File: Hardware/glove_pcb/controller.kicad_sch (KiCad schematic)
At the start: 17 parts, among them J10 ICSP, J11 IMU, J12 IMU, J9 Debug Serial, U10 MCP3008, U11 MCP3008, U8 MCP3008, U9 ATmega328PB-A

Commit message: Made most of changes from meeting
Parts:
- added C44: 0.1uF, Capacitor_SMD:C_0603_1608Metric_Pad1.08x0.95mm_HandSolder, symbol Device:C
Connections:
- net VCC_UC renamed +5V

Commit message: Finish changes according to feedback
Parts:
- removed C32: 0.1uF, Capacitor_SMD:C_0603_1608Metric_Pad1.08x0.95mm_HandSolder, symbol Device:C
- removed C33: 10uF, Capacitor_SMD:C_1206_3216Metric_Pad1.33x1.80mm_HandSolder, symbol Device:C
- added C30, C35, C36, C37, C38, C39, C40, C41, C42, C45, C46, C49, C50, C51: 0.1uF, symbol Device:C_Small
- added C43: 0.1uF, Capacitor_SMD:C_0603_1608Metric_Pad1.08x0.95mm_HandSolder, symbol Device:C
- added SW2: SW_Push, symbol Switch:SW_Push
- C44: value 0.1uF -> 10uF; footprint Capacitor_SMD:C_0603_1608Metric_Pad1.08x0.95mm_HandSolder -> Capacitor_SMD:C_1206_3216Metric_Pad1.33x1.80mm_HandSolder
- renumbered C30 to C31, C31 to C32, C28 to C33, C29 to C34, C34 to C47, C35 to C48, R34 to R30
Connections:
- net +5V: now also C44.1, C43.1
- net GND: now also C44.2, U10.7 (CH6), U10.8 (CH7), C30.1, C35.1, C36.1, C37.1, C38.1, C39.1, C40.1, C41.1, C42.1, C43.2, C45.1, C46.1, C49.1, C50.1, C51.1, SW2.2
- net POT_INDEX_1: now also C36.2
- net POT_INDEX_2: now also C37.2
- net POT_INDEX_3: now also C38.2
- net POT_MIDDLE_1: now also C39.2
- net POT_MIDDLE_2: now also C40.2
- net POT_MIDDLE_3: now also C41.2
- net POT_PINKY_1: now also C49.2
- net POT_PINKY_2: now also C50.2
- net POT_PINKY_3: now also C51.2
- net POT_RING_1: now also C42.2
- net POT_RING_2: now also C45.2
- net POT_RING_3: now also C46.2
- net POT_THUMB_1: now also C30.2
- net POT_THUMB_2: now also C35.2
- net UC_MOTOR_PMODE: no longer names the net of U9.11 (PD7)
- net UC_MOTOR_PMODE: now also SW2.1
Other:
- note added: "Emergency Stop"
- moved on the sheet: C33, C34, C47, C48, J11, J12, U11, U8

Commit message: Finish schematic updates
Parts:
- removed J10: ICSP, Connector_PinSocket_2.54mm:PinSocket_2x03_P2.54mm_Vertical, symbol Connector_Generic:Conn_02x03_Top_Bottom
- added J10: AVR-ISP-6, symbol Connector:AVR-ISP-6
- renumbered U8 to U12, U9 to U13, U10 to U14, U11 to U15
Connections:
- net +5V: now also J10.2 (VCC)
- net GND: now also J10.6 (GND)
- net MISO: now also J10.1 (MISO)
- net MOSI: now also J10.4 (MOSI)
- net RST: now also J10.5 (~{RST})
- net SCK: now also J10.3 (SCK)

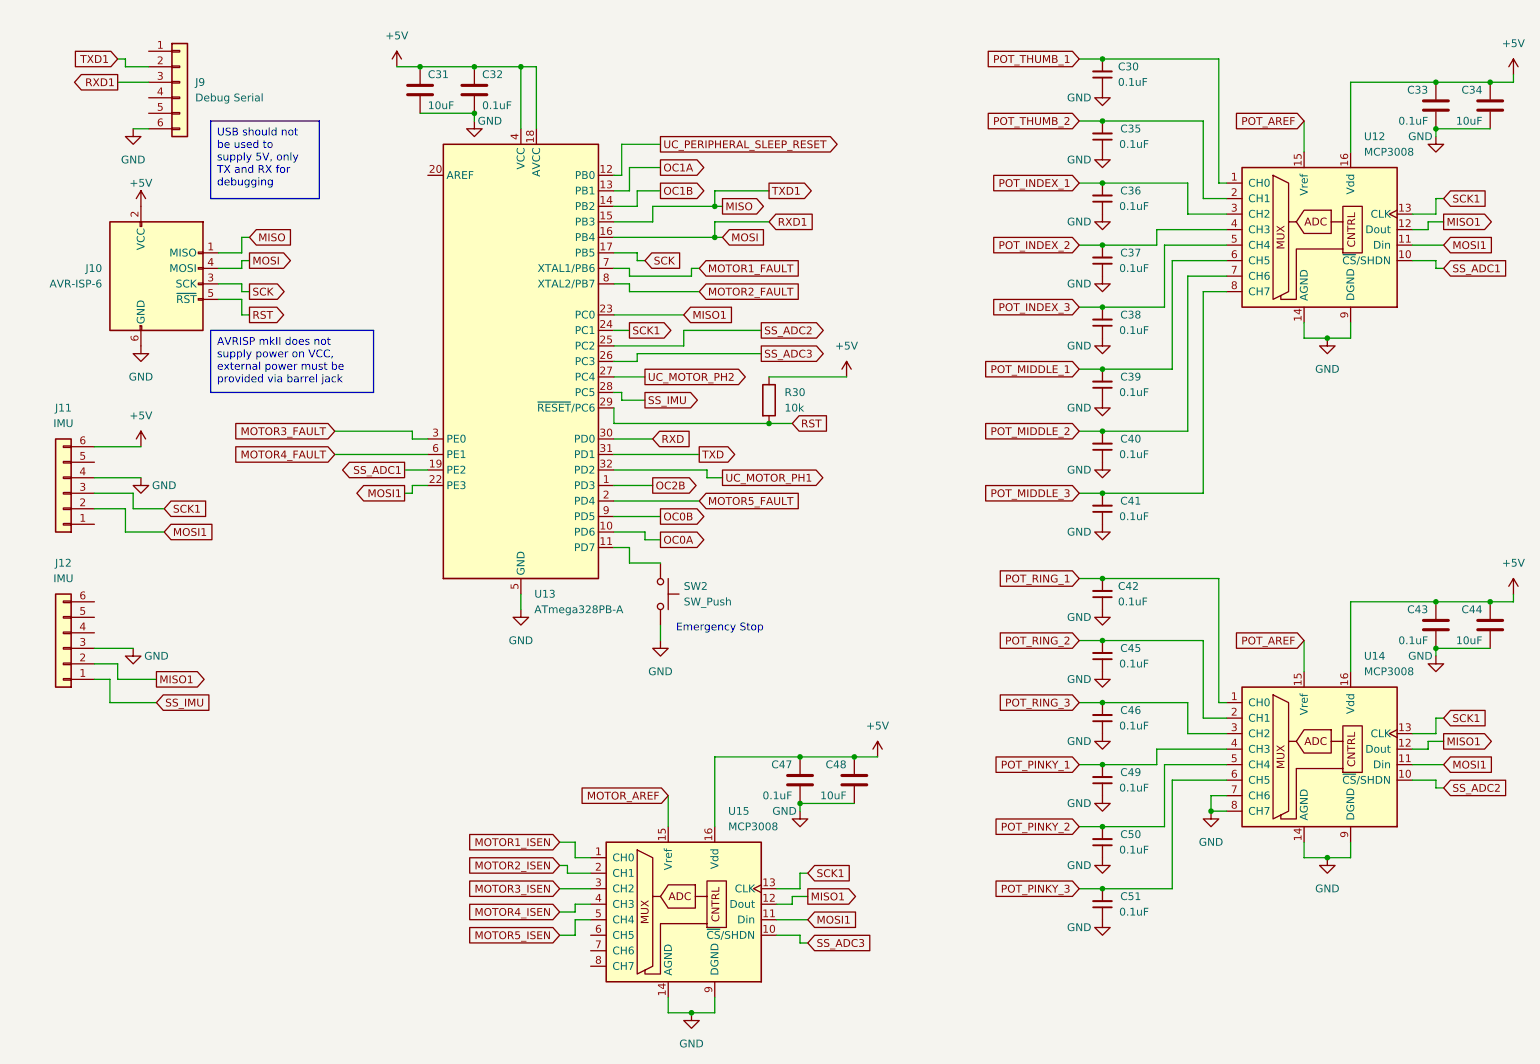
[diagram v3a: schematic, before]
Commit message: More updates to the schematic based on Dmitry's feedback
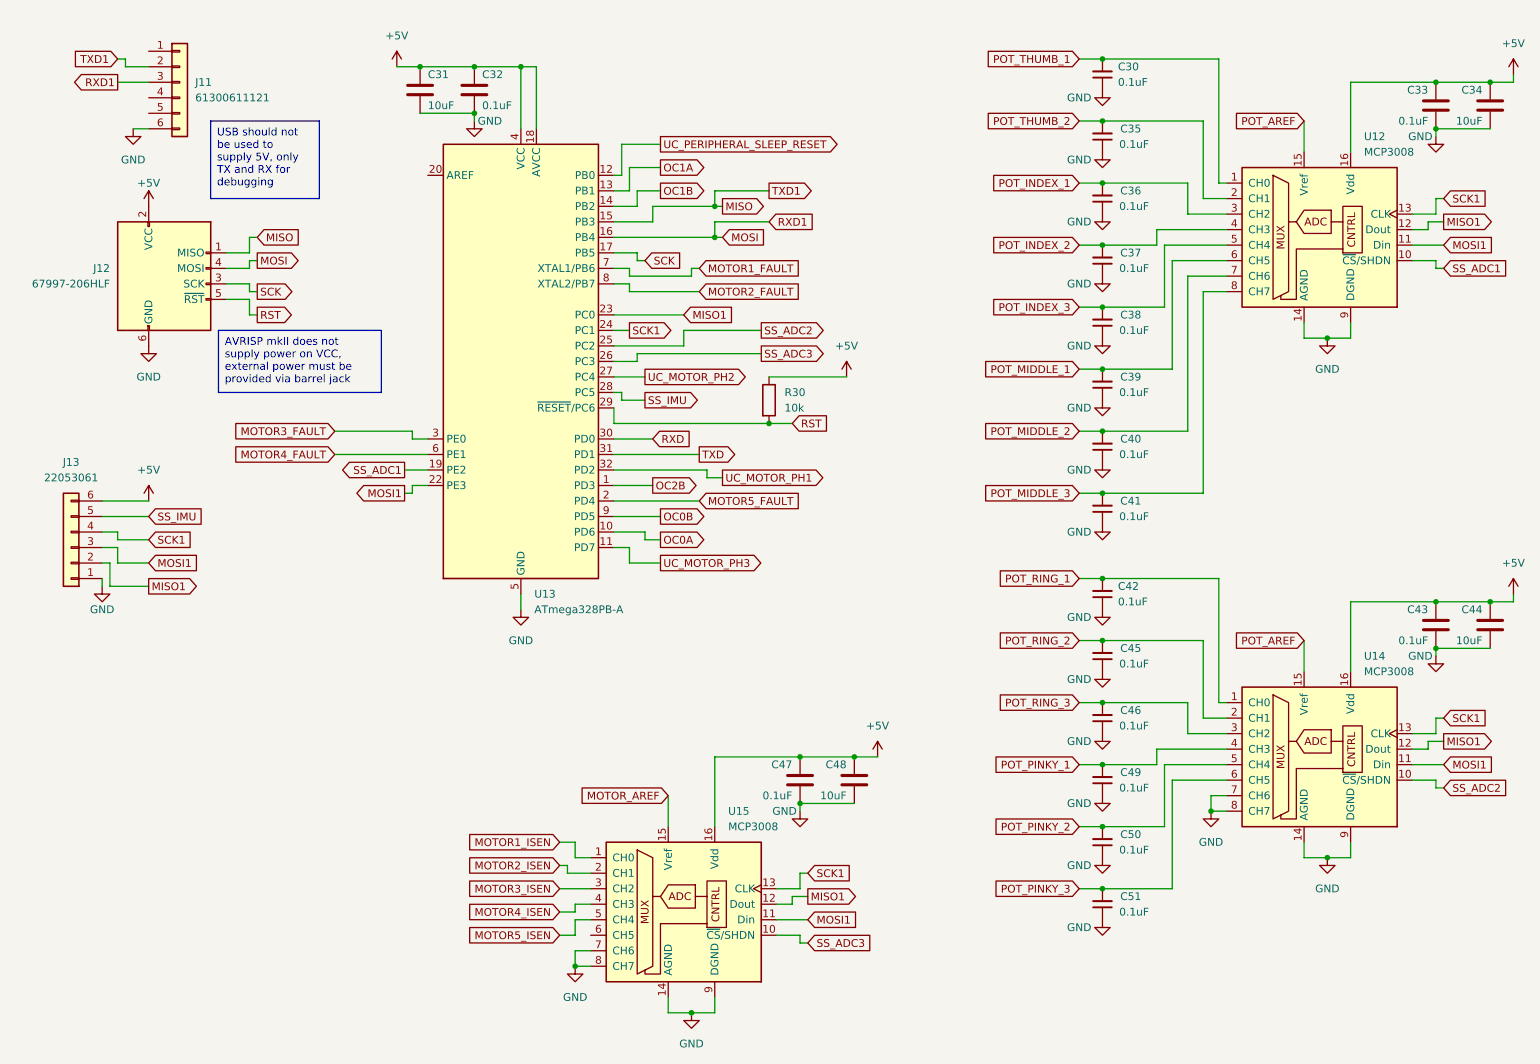
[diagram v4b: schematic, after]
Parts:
- removed J12: IMU, Connector_PinSocket_2.54mm:PinSocket_1x06_P2.54mm_Vertical, symbol Connector_Generic:Conn_01x06
- removed SW2: SW_Push, symbol Switch:SW_Push
- J11: renamed from J9; value Debug Serial -> 61300611121
- J12: renamed from J10; value AVR-ISP-6 -> 67997-206HLF
- J13: renamed from J11; value IMU -> 22053061
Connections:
- net GND: now also J13.1 (Pin_1), U15.7 (CH6), U15.8 (CH7); no longer J13.4 (Pin_4)
- net MISO1: now also J13.2 (Pin_2)
- net MOSI1: now also J13.3 (Pin_3); no longer J13.2 (Pin_2)
- net SCK1: now also J13.4 (Pin_4); no longer J13.3 (Pin_3)
- net SS_IMU: now also J13.5 (Pin_5)
- net UC_MOTOR_PH3: now reaches U13.11 (PD7)
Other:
- note removed: "Emergency Stop"
- moved on the sheet: J12, J13

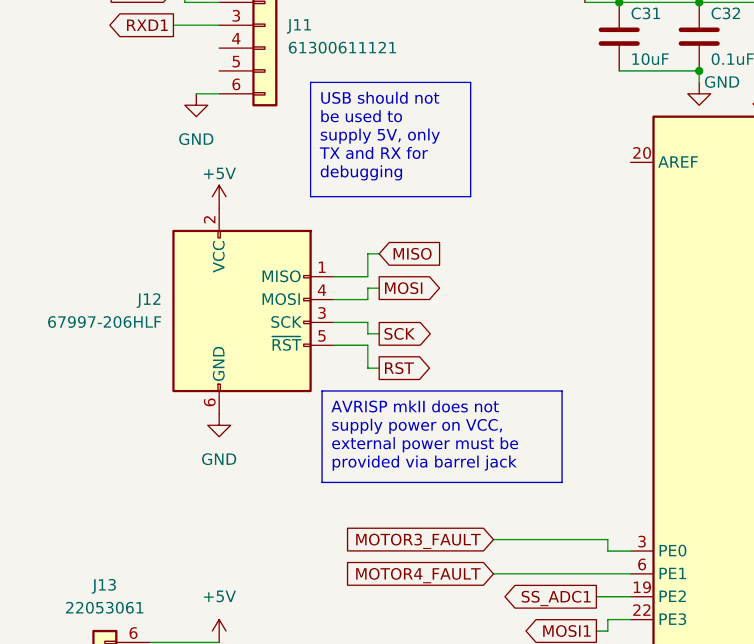
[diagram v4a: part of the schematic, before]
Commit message: Change isp pin symbol
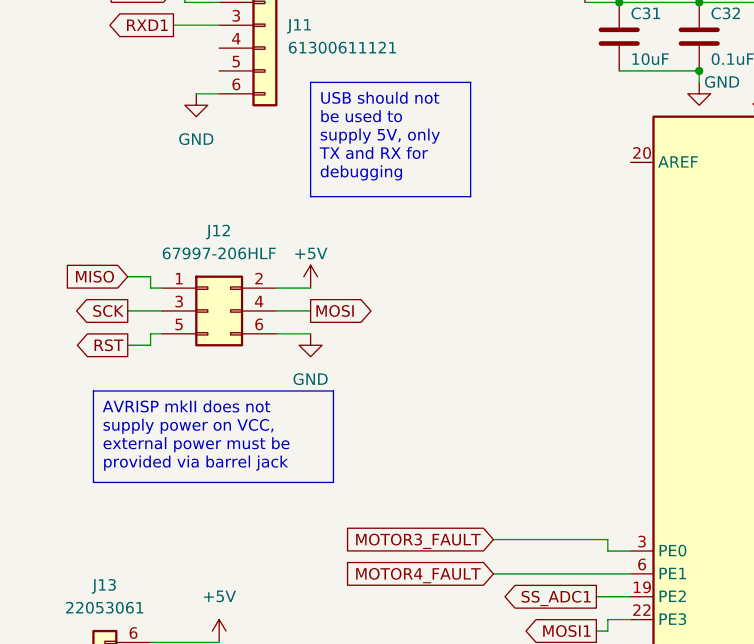
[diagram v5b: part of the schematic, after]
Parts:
- J12: symbol Connector:AVR-ISP-6 -> Connector_Generic:Conn_02x03_Odd_Even

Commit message: Assign footprints and import all parts into pcb editor
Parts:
- C30, C35, C36, C37, C38, C39, C40, C41, C42, C45, C46, C49, C50, C51: footprint (none) -> Capacitor_SMD:C_0603_1608Metric_Pad1.08x0.95mm_HandSolder
- J12: footprint (none) -> Connector_PinHeader_2.54mm:PinHeader_2x03_P2.54mm_Vertical
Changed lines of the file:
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@@
       (effects (font (size 1.27 1.27)) (justify right))
     )
-    (property "Footprint" "" (at 190.5 138.43 0)
+    (property "Footprint" "Capacitor_SMD:C_0603_1608Metric_Pad1.08x0.95mm_HandSolder" (at 190.5 138.43 0)
       (effects (font (size 1.27 1.27)) hide)
     )
@@
       (effects (font (size 1.27 1.27)) (justify right))
     )
-    (property "Footprint" "" (at 190.5 148.59 0)
+    (property "Footprint" "Capacitor_SMD:C_0603_1608Metric_Pad1.08x0.95mm_HandSolder" (at 190.5 148.59 0)
       (effects (font (size 1.27 1.27)) hide)
     )
@@
       (effects (font (size 1.27 1.27)) (justify right))
     )
-    (property "Footprint" "" (at 190.5 128.27 0)
+    (property "Footprint" "Capacitor_SMD:C_0603_1608Metric_Pad1.08x0.95mm_HandSolder" (at 190.5 128.27 0)
       (effects (font (size 1.27 1.27)) hide)
     )
@@
       (effects (font (size 1.27 1.27)) (justify right))
     )
-    (property "Footprint" "" (at 190.5 118.11 0)
+    (property "Footprint" "Capacitor_SMD:C_0603_1608Metric_Pad1.08x0.95mm_HandSolder" (at 190.5 118.11 0)
       (effects (font (size 1.27 1.27)) hide)
     )
@@
       (effects (font (size 1.27 1.27)) (justify right))
     )
-    (property "Footprint" "" (at 190.5 107.95 0)
+    (property "Footprint" "Capacitor_SMD:C_0603_1608Metric_Pad1.08x0.95mm_HandSolder" (at 190.5 107.95 0)
       (effects (font (size 1.27 1.27)) hide)
     )
@@
       (effects (font (size 1.27 1.27)))
     )
-    (property "Footprint" "" (at 33.02 55.88 0)
+    (property "Footprint" "Connector_PinHeader_2.54mm:PinHeader_2x03_P2.54mm_Vertical" (at 33.02 55.88 0)
       (effects (font (size 1.27 1.27)) hide)
     )
@@
       (effects (font (size 1.27 1.27)) (justify right))
     )
-    (property "Footprint" "" (at 190.5 33.02 0)
+    (property "Footprint" "Capacitor_SMD:C_0603_1608Metric_Pad1.08x0.95mm_HandSolder" (at 190.5 33.02 0)
       (effects (font (size 1.27 1.27)) hide)
     )
@@
       (effects (font (size 1.27 1.27)) (justify right))
     )
-    (property "Footprint" "" (at 190.5 73.66 0)
+    (property "Footprint" "Capacitor_SMD:C_0603_1608Metric_Pad1.08x0.95mm_HandSolder" (at 190.5 73.66 0)
       (effects (font (size 1.27 1.27)) hide)
     )
@@
       (effects (font (size 1.27 1.27)) (justify right))
     )
-    (property "Footprint" "" (at 190.5 22.86 0)
+    (property "Footprint" "Capacitor_SMD:C_0603_1608Metric_Pad1.08x0.95mm_HandSolder" (at 190.5 22.86 0)
       (effects (font (size 1.27 1.27)) hide)
     )
@@
       (effects (font (size 1.27 1.27)) (justify right))
     )
-    (property "Footprint" "" (at 190.5 158.75 0)
+    (property "Footprint" "Capacitor_SMD:C_0603_1608Metric_Pad1.08x0.95mm_HandSolder" (at 190.5 158.75 0)
       (effects (font (size 1.27 1.27)) hide)
     )
@@
       (effects (font (size 1.27 1.27)) (justify right))
     )
-    (property "Footprint" "" (at 190.5 93.98 0)
+    (property "Footprint" "Capacitor_SMD:C_0603_1608Metric_Pad1.08x0.95mm_HandSolder" (at 190.5 93.98 0)
       (effects (font (size 1.27 1.27)) hide)
     )
@@
       (effects (font (size 1.27 1.27)) (justify right))
     )
-    (property "Footprint" "" (at 190.5 53.34 0)
+    (property "Footprint" "Capacitor_SMD:C_0603_1608Metric_Pad1.08x0.95mm_HandSolder" (at 190.5 53.34 0)
       (effects (font (size 1.27 1.27)) hide)
     )
@@
       (effects (font (size 1.27 1.27)) (justify right))
     )
-    (property "Footprint" "" (at 190.5 83.82 0)
+    (property "Footprint" "Capacitor_SMD:C_0603_1608Metric_Pad1.08x0.95mm_HandSolder" (at 190.5 83.82 0)
       (effects (font (size 1.27 1.27)) hide)
     )
@@
       (effects (font (size 1.27 1.27)) (justify right))
     )
-    (property "Footprint" "" (at 190.5 43.18 0)
+    (property "Footprint" "Capacitor_SMD:C_0603_1608Metric_Pad1.08x0.95mm_HandSolder" (at 190.5 43.18 0)
       (effects (font (size 1.27 1.27)) hide)
     )
@@
       (effects (font (size 1.27 1.27)) (justify right))
     )
-    (property "Footprint" "" (at 190.5 63.5 0)
-      (effects (font (size 1.27 1.27)) hide)
-    )
+    (property "Footprint" "Capacitor_SMD:C_0603_1608Metric_Pad1.08x0.95mm_HandSolder" (at 190.5 63.5 0)
+      (effects (font (size 1.27 1.27)) hide)
+    )

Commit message: More placing
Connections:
- net GND: now also U12.8 (CH7); no longer U14.7 (CH6)
- net POT_MIDDLE_3: now also U14.1 (CH0); no longer U12.8 (CH7)
- net POT_PINKY_1: now also U14.5 (CH4); no longer U14.4 (CH3)
- net POT_PINKY_2: now also U14.6 (CH5); no longer U14.5 (CH4)
- net POT_PINKY_3: now also U14.7 (CH6); no longer U14.6 (CH5)
- net POT_RING_1: now also U14.2 (CH1); no longer U14.1 (CH0)
- net POT_RING_2: now also U14.3 (CH2); no longer U14.2 (CH1)
- net POT_RING_3: now also U14.4 (CH3); no longer U14.3 (CH2)
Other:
- moved on the sheet: C41, C42, C45, C46, C49, C50, C51

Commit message: Re-placing with new outline
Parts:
- J13: footprint Connector_PinSocket_2.54mm:PinSocket_1x06_P2.54mm_Vertical -> Connector_PinSocket_2.54mm:PinSocket_1x06_P2.54mm_Horizontal
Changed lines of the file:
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@@
       (effects (font (size 1.27 1.27)))
     )
-    (property "Footprint" "Connector_PinSocket_2.54mm:PinSocket_1x06_P2.54mm_Vertical" (at 21.59 100.33 0)
+    (property "Footprint" "Connector_PinSocket_2.54mm:PinSocket_1x06_P2.54mm_Horizontal" (at 21.59 100.33 0)
       (effects (font (size 1.27 1.27)) hide)
     )
